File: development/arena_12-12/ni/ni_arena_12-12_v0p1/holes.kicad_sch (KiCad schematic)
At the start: 4 parts

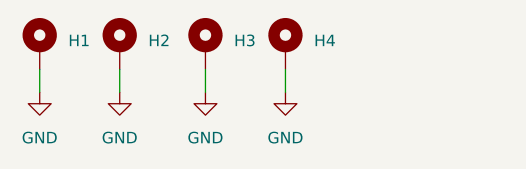
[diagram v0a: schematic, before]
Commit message: Finished initial schematic and layout for 12-12 NI arena (without voltage regulators).
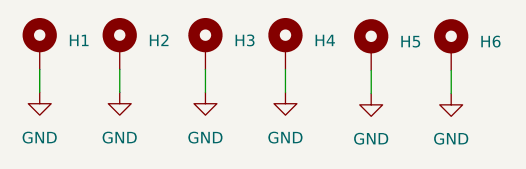
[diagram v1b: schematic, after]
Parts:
- added H5, H6: MountingHole_Pad, MountingHole:MountingHole_4.5mm_Pad, symbol Mechanical:MountingHole_Pad
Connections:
- net GND: now also H5.1, H6.1
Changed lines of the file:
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@@
 (kicad_sch (version 20230121) (generator eeschema)
   (paper "A4")
+  (wire (pts (xy 78.105 32.766) (xy 78.105 35.306))
+    (stroke (width 0) (type default))
+  )
   (wire (pts (xy 41.275 32.639) (xy 41.275 35.179))
     (stroke (width 0) (type default))
   )
+  (wire (pts (xy 86.995 32.766) (xy 86.995 35.306))
+    (stroke (width 0) (type default))
+  )
   (wire (pts (xy 59.69 32.639) (xy 59.69 35.179))
     (stroke (width 0) (type default))
@@
   (wire (pts (xy 50.165 32.639) (xy 50.165 35.179))
     (stroke (width 0) (type default))
+  )
+  (symbol (lib_id "power:GND") (at 86.995 35.306 0) (mirror y) (unit 1)
+    (in_bom yes) (on_board yes) (dnp no) (fields_autoplaced)
+    (property "Reference" "#PWR020" (at 86.995 41.656 0)
+      (effects (font (size 1.27 1.27)) hide)
+    )
+    (property "Value" "GND" (at 86.995 40.386 0)
+      (effects (font (size 1.27 1.27)))
+    )
+    (property "Footprint" "" (at 86.995 35.306 0)
+      (effects (font (size 1.27 1.27)) hide)
+    )
+    (property "Datasheet" "" (at 86.995 35.306 0)
+      (effects (font (size 1.27 1.27)) hide)
+    )
+    (pin "1")
+    (instances
+      (project "ni_arena_12-12"
+        (path "/a2511654-3a17-43f1-8b9e-c45e375533dc/24a22302-295f-4a79-8162-dc1243f756aa"
+          (reference "#PWR020") (unit 1)
+        )
+      )
+    )
   )
   (symbol (lib_id "power:GND") (at 68.58 35.179 0) (mirror y) (unit 1)
@@
         )
       )
+    )
+  )
+  (symbol (lib_id "Mechanical:MountingHole_Pad") (at 86.995 30.226 0) (unit 1)
+    (in_bom yes) (on_board yes) (dnp no) (fields_autoplaced)
+    (property "Reference" "H6" (at 90.17 29.591 0)
+      (effects (font (size 1.27 1.27)) (justify left))
+    )
+    (property "Value" "MountingHole_Pad" (at 90.17 30.861 0)
+      (effects (font (size 1.27 1.27)) (justify left) hide)
+    )
+    (property "Footprint" "MountingHole:MountingHole_4.5mm_Pad" (at 86.995 30.226 0)
+      (effects (font (size 1.27 1.27)) hide)
+    )
+    (property "Datasheet" "~" (at 86.995 30.226 0)
+      (effects (font (size 1.27 1.27)) hide)
+    )
+    (pin "1")
+    (instances
+      (project "ni_arena_12-12"
+        (path "/a2511654-3a17-43f1-8b9e-c45e375533dc/24a22302-295f-4a79-8162-dc1243f756aa"
+          (reference "H6") (unit 1)
+        )
+      )
+    )
+  )
+  (symbol (lib_id "Mechanical:MountingHole_Pad") (at 78.105 30.226 0) (unit 1)
+    (in_bom yes) (on_board yes) (dnp no) (fields_autoplaced)
+    (property "Reference" "H5" (at 81.28 29.591 0)
+      (effects (font (size 1.27 1.27)) (justify left))
+    )
+    (property "Value" "MountingHole_Pad" (at 81.28 30.861 0)
+      (effects (font (size 1.27 1.27)) (justify left) hide)
+    )
+    (property "Footprint" "MountingHole:MountingHole_4.5mm_Pad" (at 78.105 30.226 0)
+      (effects (font (size 1.27 1.27)) hide)
+    )
+    (property "Datasheet" "~" (at 78.105 30.226 0)
+      (effects (font (size 1.27 1.27)) hide)
+    )
+    (pin "1")
+    (instances
+      (project "ni_arena_12-12"
+        (path "/a2511654-3a17-43f1-8b9e-c45e375533dc/24a22302-295f-4a79-8162-dc1243f756aa"
+          (reference "H5") (unit 1)
+        )
+      )
+    )
+  )
+  (symbol (lib_id "power:GND") (at 78.105 35.306 0) (mirror y) (unit 1)
+    (in_bom yes) (on_board yes) (dnp no) (fields_autoplaced)
+    (property "Reference" "#PWR019" (at 78.105 41.656 0)
+      (effects (font (size 1.27 1.27)) hide)
+    )
+    (property "Value" "GND" (at 78.105 40.386 0)
+      (effects (font (size 1.27 1.27)))
+    )
+    (property "Footprint" "" (at 78.105 35.306 0)
+      (effects (font (size 1.27 1.27)) hide)
+    )
+    (property "Datasheet" "" (at 78.105 35.306 0)
+      (effects (font (size 1.27 1.27)) hide)
+    )
+    (pin "1")
+    (instances
+      (project "ni_arena_12-12"
+        (path "/a2511654-3a17-43f1-8b9e-c45e375533dc/24a22302-295f-4a79-8162-dc1243f756aa"
+          (reference "#PWR019") (unit 1)
+        )
+      )
